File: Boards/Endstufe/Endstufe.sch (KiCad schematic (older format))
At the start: 54 parts, among them J1 HV In, J2 Relais, J3 NF_In, J4 Trafo, K1 G6E, P4 6V3_AC, P6 6V3_DC, P8 Bias, T1 KT88, T2 KT88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

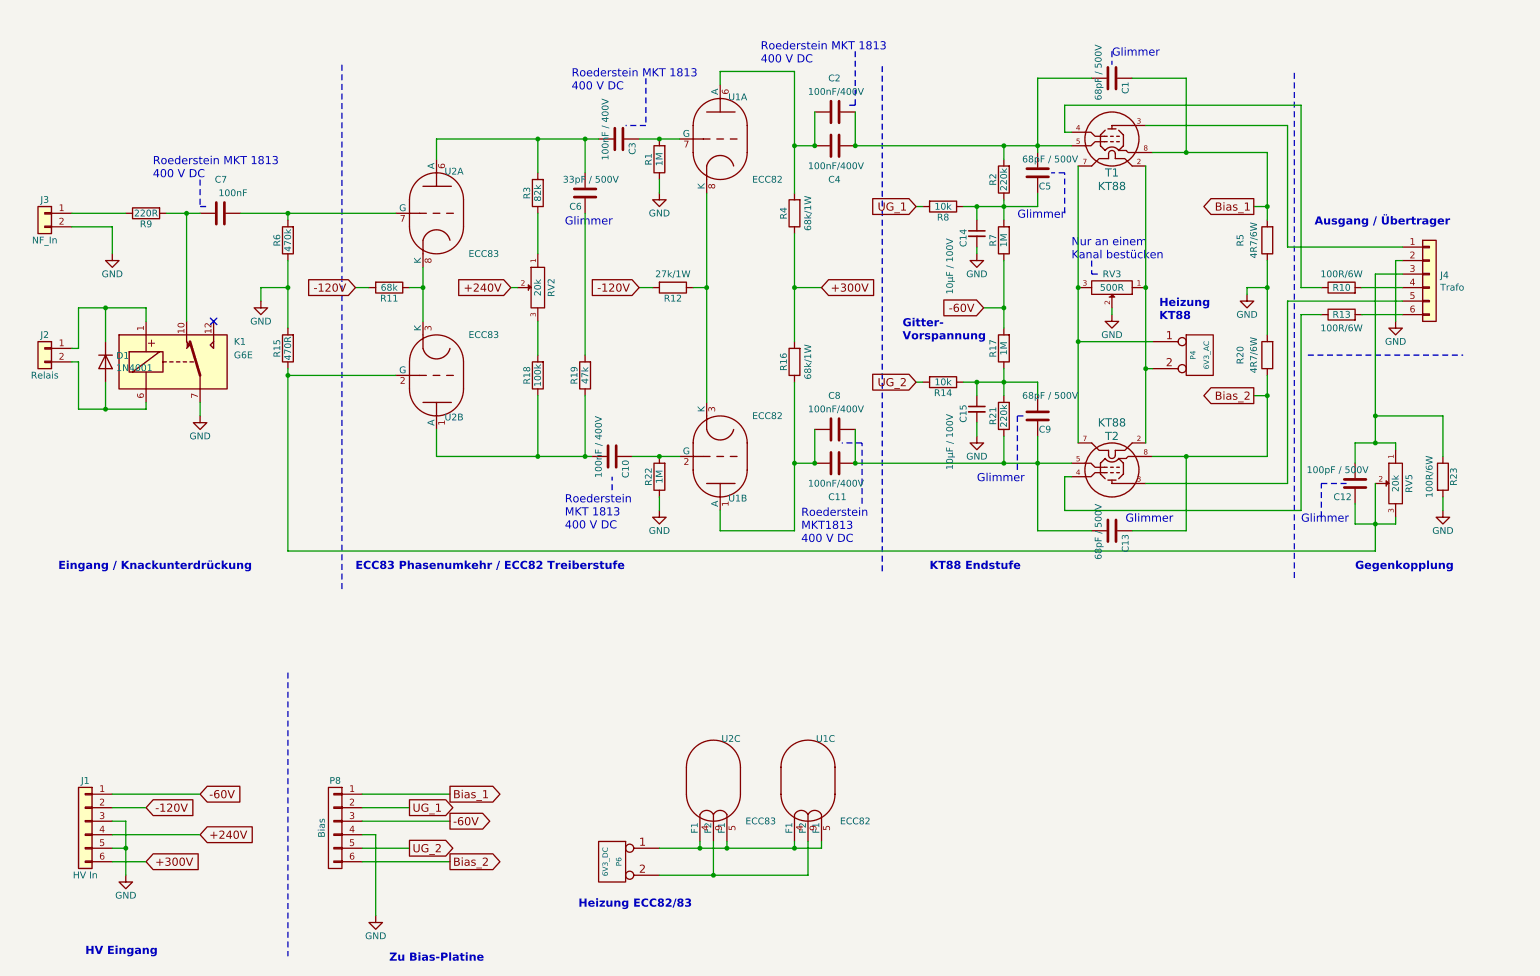
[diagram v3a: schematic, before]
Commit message: Reworked Delay + Layout changed
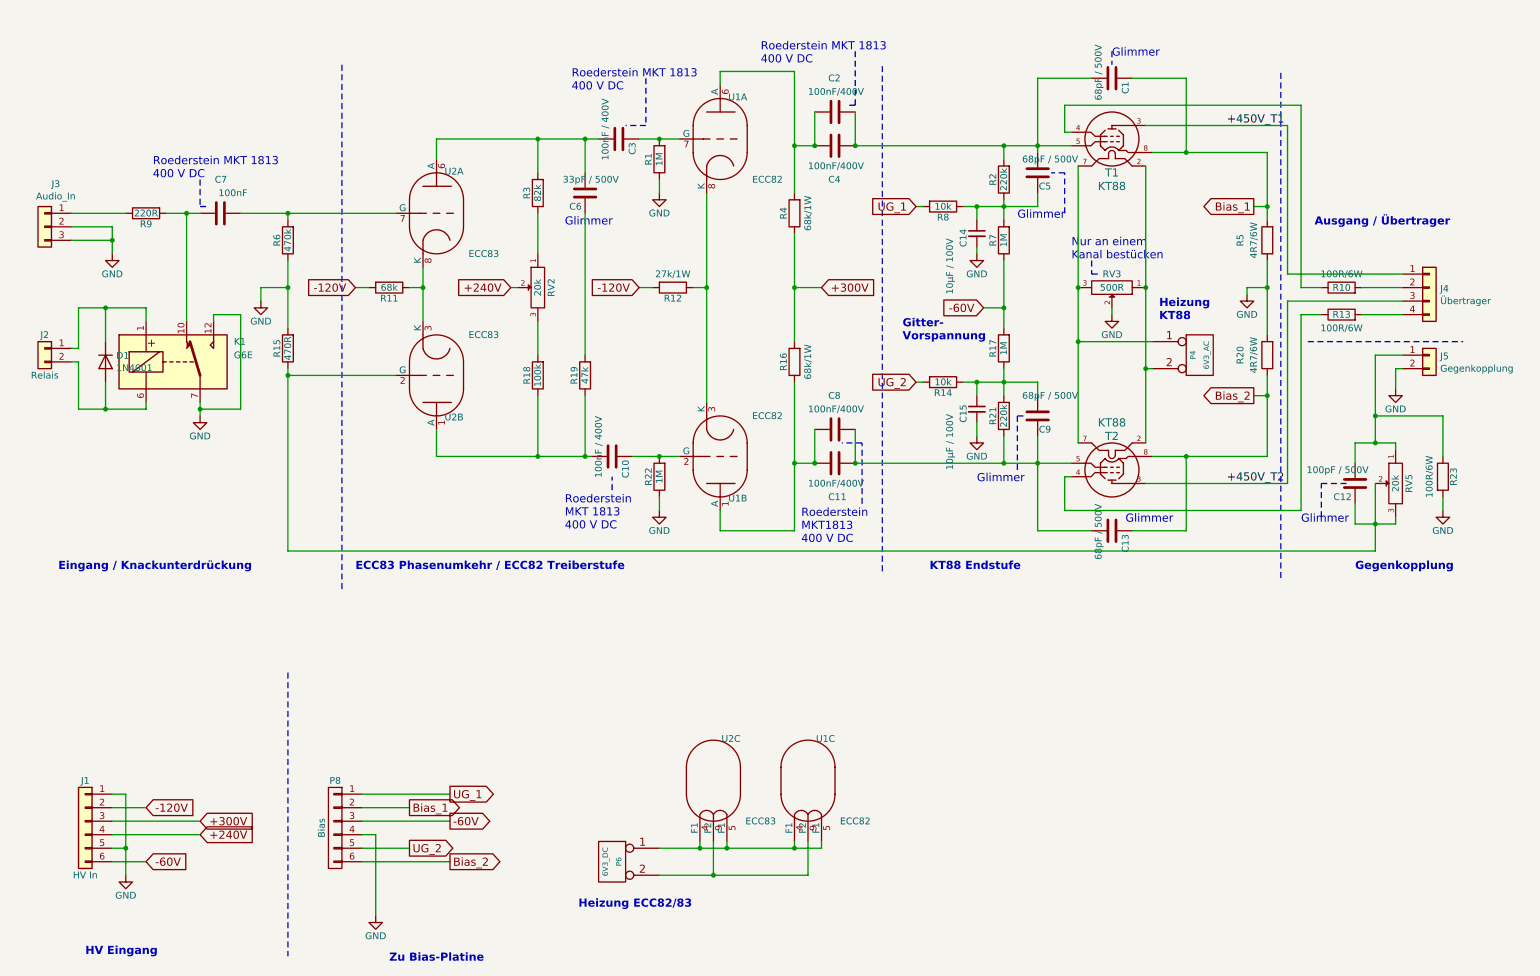
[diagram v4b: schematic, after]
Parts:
- removed J3: NF_In, Connector_JST:JST_EH_B2B-EH-A_1x02_P2.50mm_Vertical, symbol Endstufe-rescue:Conn_01x02
- removed J4: Trafo, Connector_TE-Connectivity:TE_MATE-N-LOK_1-770875-x_2x03_P4.14mm_Vertical, symbol Connector_Generic:Conn_01x06
- added J3: Audio_In, Connector_JST:JST_EH_B3B-EH-A_1x03_P2.50mm_Vertical, symbol Connector_Generic:Conn_01x03
- added J4: Übertrager, Connector_TE-Connectivity:TE_MATE-N-LOK_350211-1_1x04_P5.08mm_Vertical, symbol Connector_Generic:Conn_01x04
- added J5: Gegenkopplung, Connector_TE-Connectivity:TE_MATE-N-LOK_1-770866-x_1x02_P4.14mm_Vertical, symbol Connector_Generic:Conn_01x02
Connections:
- net +300V: now also J1.3 (Pin_3); no longer J1.6 (Pin_6)
- net -60V: now also J1.6 (Pin_6); no longer J1.1 (Pin_1)
- net Bias_1: now also P8.2 (P2); no longer P8.1 (P1)
- net GND: now also J1.1 (Pin_1), K1.12, J3.2 (Pin_2), J3.3 (Pin_3), J5.2 (Pin_2); no longer J1.3 (Pin_3)
- net UG_1: now also P8.1 (P1); no longer P8.2 (P2)
- net +450V_T1: now reaches T1.3 (a)
- net +450V_T1: now also J4.1 (Pin_1)
- net +450V_T2: now reaches T2.3 (a)
- net +450V_T2: now also J4.3 (Pin_3)
- net at C12.2, R23.1, RV5.1: now also J5.1 (Pin_1)
- net at R10.2: now also J4.2 (Pin_2)
- net at R13.2: now also J4.4 (Pin_4)
- net at R9.1: now also J3.1 (Pin_1)
- no-connect marks 1 -> 0
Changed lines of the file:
@@
 Wire Wire Line
 	11050 3600 10550 3600
-Connection ~ 10550 3600
 Wire Wire Line
 	11050 4300 11050 4200
@@
 Connection ~ 5650 7000
 Wire Wire Line
-	1200 2200 1200 2400
-Wire Wire Line
-	900  2200 1200 2200
+	1200 2200 1200 2300
 Wire Notes Line
 	6900 4750 6900 1000
@@
 	1    0    0    -1
 $EndComp
-Text GLabel 1450 6900 2    60   Input ~ 0
+Text GLabel 1850 6600 2    60   Input ~ 0
 +300V
 Text GLabel 1850 6700 2    60   Input ~ 0
@@
 	1    0    0    -1
 $EndComp
-Text GLabel 3400 6500 2    60   Output ~ 0
+Text GLabel 3700 6400 2    60   Output ~ 0
 UG_1
 Text GLabel 3400 6800 2    60   Output ~ 0
 UG_2
-Text GLabel 3700 6400 2    60   Output ~ 0
+Text GLabel 3400 6500 2    60   Output ~ 0
 Bias_1
 Text GLabel 3700 6900 2    60   Output ~ 0
@@
 	2150 2100 2500 2100
 Wire Wire Line
-	3700 6400 3050 6400
-Wire Wire Line
 	3050 6700 3150 6700
 Wire Wire Line
@@
 	1450 3550 1450 3500
 Wire Wire Line
-	1850 3600 1850 3500
+	1850 3600 1850 3550
 $Comp
 L Endstufe-rescue:Conn_01x06 J1
@@
 $EndComp
 $Comp
-L Endstufe-rescue:Conn_01x02 J3
-U 1 1 5A92D98F
-P 700 2100
-F 0 "J3" H 700 2200 50  0000 C CNN
-F 1 "NF_In" H 700 1900 50  0000 C CNN
-F 2 "Connector_JST:JST_EH_B2B-EH-A_1x02_P2.50mm_Vertical" H 700 2100 50  0001 C CNN
-F 3 "" H 700 2100 50  0001 C CNN
-	1    700  2100
-	-1   0    0    -1
-$EndComp
-$Comp
 L Endstufe-rescue:Conn_01x02 J2
 U 1 1 5A92DE06
@@
 Wire Wire Line
 	9750 3450 9750 3900
-NoConn ~ 1950 2900
 Wire Wire Line
 	1750 2100 1850 2100
@@
 Connection ~ 6700 1600
 Connection ~ 6700 3950
-$Comp
-L Connector_Generic:Conn_01x06 J4
-U 1 1 5CC18566
-P 10950 2550
-F 0 "J4" H 11030 2542 50  0000 L CNN
-F 1 "Trafo" H 11030 2451 50  0000 L CNN
-F 2 "Connector_TE-Connectivity:TE_MATE-N-LOK_1-770875-x_2x03_P4.14mm_Vertical" H 10950 2550 50  0001 C CNN
-F 3 "~" H 10950 2550 50  0001 C CNN
-	1    10950 2550
-	1    0    0    -1
-$EndComp
-Wire Wire Line
-	9900 1450 9900 2350
-Wire Wire Line
-	10750 2350 9900 2350
+Wire Wire Line
+	9900 1450 9900 2550
+Wire Wire Line
+	10750 2550 9900 2550
 Wire Wire Line
 	10450 2650 10750 2650
-$Comp
-L Endstufe-rescue:GND #PWR0101
-U 1 1 5CCAF2A5
-P 10700 2900
-F 0 "#PWR0101" H 10700 2650 50  0001 C CNN
-F 1 "GND" H 10700 2750 50  0000 C CNN
-F 2 "" H 10700 2900 60  0000 C CNN
-F 3 "" H 10700 2900 60  0000 C CNN
-	1    10700 2900
-	1    0    0    -1
-$EndComp
-Wire Wire Line
-	10700 2450 10750 2450
-Wire Wire Line
-	10700 2450 10700 2900
 Wire Wire Line
 	10750 2850 10450 2850
@@
 Heizung\nKT88
 Wire Notes Line
-	9950 4800 9950 1050
-Wire Notes Line
-	10050 3150 11200 3150
+	9850 4800 9850 1050
+Wire Notes Line
+	10050 3050 11200 3050
 Wire Notes Line
 	2500 5500 2500 7600
@@
 Wire Wire Line
 	3050 6800 3400 6800
-Wire Wire Line
-	3050 6500 3400 6500
 Wire Wire Line
 	7600 2400 7600 2350
@@
 	1450 6500 1200 6500
 Wire Wire Line
-	1200 6600 1300 6600
-Wire Wire Line
-	1300 6600 1300 6800
-Wire Wire Line
 	1200 6800 1300 6800
-Connection ~ 1300 6800
 Wire Wire Line
 	1300 6800 1300 7000
-Text GLabel 1850 6400 2    60   Input ~ 0
+Text GLabel 1450 6900 2    60   Input ~ 0
 -60V
-Wire Wire Line
-	1850 6400 1200 6400
 Wire Wire Line
 	7800 2450 7800 2800
@@
 Wire Notes Line
 	8450 2550 8500 2550
-Wire Wire Line
-	10550 2550 10750 2550
-Wire Wire Line
-	10550 2550 10550 3600
+$Comp
+L Connector_Generic:Conn_01x04 J4
+U 1 1 60906A39
+P 10950 2650
+F 0 "J4" H 11030 2642 50  0000 L CNN
+F 1 "Übertrager" H 11030 2551 50  0000 L CNN
+F 2 "Connector_TE-Connectivity:TE_MATE-N-LOK_350211-1_1x04_P5.08mm_Vertical" H 10950 2650 50  0001 C CNN
+F 3 "~" H 10950 2650 50  0001 C CNN
+	1    10950 2650
+	1    0    0    -1
+$EndComp
+$Comp
+L Connector_Generic:Conn_01x02 J5
+U 1 1 60914273
+P 10950 3150
+F 0 "J5" H 11030 3142 50  0000 L CNN
+F 1 "Gegenkopplung" H 11030 3051 50  0000 L CNN
+F 2 "Connector_TE-Connectivity:TE_MATE-N-LOK_1-770866-x_1x02_P4.14mm_Vertical" H 10950 3150 50  0001 C CNN
+F 3 "~" H 10950 3150 50  0001 C CNN
+	1    10950 3150
+	1    0    0    -1
+$EndComp
+Connection ~ 10550 3600
+$Comp
+L Endstufe-rescue:GND #PWR0101
+U 1 1 60920978
+P 10700 3400
+F 0 "#PWR0101" H 10700 3150 50  0001 C CNN
+F 1 "GND" H 10700 3250 50  0000 C CNN
+F 2 "" H 10700 3400 60  0000 C CNN
+F 3 "" H 10700 3400 60  0000 C CNN
+	1    10700 3400
+	1    0    0    -1
+$EndComp
+Wire Wire Line
+	10750 3150 10550 3150
+Wire Wire Line
+	10550 3150 10550 3600
+Wire Wire Line
+	10750 3250 10700 3250
+Wire Wire Line
+	10700 3250 10700 3400
+Wire Wire Line
+	1850 6600 1200 6600
+Wire Wire Line
+	1300 6800 1300 6400
+Wire Wire Line
+	1300 6400 1200 6400
+Connection ~ 1300 6800
+Wire Wire Line
+	3400 6500 3050 6500
+Wire Wire Line
+	3050 6400 3700 6400
+Wire Wire Line
+	1850 3550 2150 3550
+Wire Wire Line
+	2150 3550 2150 2850
+Wire Wire Line
+	2150 2850 1950 2850
+Wire Wire Line
+	1950 2850 1950 2900
+Connection ~ 1850 3550
+Wire Wire Line
+	1850 3550 1850 3500
+$Comp
+L Connector_Generic:Conn_01x03 J3
+U 1 1 6099AC4C
+P 700 2200
+F 0 "J3" H 618 2517 50  0000 C CNN
+F 1 "Audio_In" H 618 2426 50  0000 C CNN
+F 2 "Connector_JST:JST_EH_B3B-EH-A_1x03_P2.50mm_Vertical" H 700 2200 50  0001 C CNN
+F 3 "~" H 700 2200 50  0001 C CNN
+	1    700  2200
+	-1   0    0    -1
+$EndComp
+Wire Wire Line
+	900  2300 1200 2300
+Connection ~ 1200 2300
+Wire Wire Line
+	1200 2300 1200 2400
+Wire Wire Line
+	1200 2200 900  2200
+Text Label 9450 1450 0    60   ~ 0
++450V_T1
+Text Label 9450 4100 0    60   ~ 0
++450V_T2
 $EndSCHEMATC

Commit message: Work in progess - many LAyour changes
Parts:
- removed C14, C15: 10µF / 100V, Capacitor_THT:C_Radial_D6.3mm_H5.0mm_P2.50mm, symbol Endstufe-rescue:C_Small
- removed P4: 6V3_AC, Connector_TE-Connectivity:TE_MATE-N-LOK_1-770866-x_1x02_P4.14mm_Vertical, symbol Endstufe-rescue:CONN_2
- removed P8: Bias, Connector_PinHeader_2.54mm:PinHeader_2x03_P2.54mm_Vertical, symbol Endstufe-rescue:CONN_01X06
- removed RV3: 500R, Potentiometer_THT:Potentiometer_Piher_PT-10-V10_Vertical, symbol Endstufe-rescue:POT-RESCUE-Endstufe
- added C14, C15: 10µF/100V, Capacitor_THT:CP_Radial_D6.3mm_P2.50mm, symbol Device:CP_Small
- added J10: 240V VU, Connector_TE-Connectivity:TE_MATE-N-LOK_1-770866-x_1x02_P4.14mm_Vertical, symbol Connector_Generic:Conn_01x02
- added J6: 12V out, Connector_Molex:Molex_KK-254_AE-6410-02A_1x02_P2.54mm_Vertical, symbol Connector_Generic:Conn_01x02
- added J7: Conn_01x08, Connector_PinHeader_2.54mm:PinHeader_2x04_P2.54mm_Vertical, symbol Connector_Generic:Conn_01x08
- added J8: 12V In, Connector_Molex:Molex_KK-254_AE-6410-02A_1x02_P2.54mm_Vertical, symbol Connector_Generic:Conn_01x02
- added J9: VU-Meter, Connector_TE-Connectivity:TE_MATE-N-LOK_1-770866-x_1x02_P4.14mm_Vertical, symbol Connector_Generic:Conn_01x02
- added P1, P2: 6V3_AC, Connector_TE-Connectivity:TE_MATE-N-LOK_1-770866-x_1x02_P4.14mm_Vertical, symbol Endstufe-rescue:CONN_2
- C6: footprint Capacitor_THT:C_Disc_D6.0mm_W2.5mm_P5.00mm -> Capacitor_THT:C_Disc_D6.0mm_W4.4mm_P5.00mm
- C7: footprint Capacitor_THT:C_Disc_D3.0mm_W2.0mm_P2.50mm -> Capacitor_THT:C_Axial_L22.0mm_D9.5mm_P27.50mm_Horizontal
- C9: footprint Capacitor_THT:C_Disc_D7.5mm_W2.5mm_P5.00mm -> Capacitor_THT:C_Disc_D7.5mm_W4.4mm_P5.00mm
- R10, R13, R20, R23, R5: footprint Resistor_THT:R_Axial_Power_L25.0mm_W9.0mm_P30.48mm -> Resistor_THT:R_Axial_DIN0922_L20.0mm_D9.0mm_P25.40mm_Horizontal
- R11: value 68k -> 68k/1W; footprint Resistor_THT:R_Axial_DIN0207_L6.3mm_D2.5mm_P10.16mm_Horizontal -> Resistor_THT:R_Axial_DIN0207_L6.3mm_D2.5mm_P15.24mm_Horizontal
- R12: footprint Resistor_THT:R_Axial_DIN0414_L11.9mm_D4.5mm_P20.32mm_Horizontal -> Resistor_THT:R_Axial_DIN0207_L6.3mm_D2.5mm_P15.24mm_Horizontal
- R16, R4: footprint Resistor_THT:R_Axial_DIN0414_L11.9mm_D4.5mm_P15.24mm_Horizontal -> Resistor_THT:R_Axial_DIN0207_L6.3mm_D2.5mm_P10.16mm_Horizontal
- RV2, RV5: footprint Potentiometer_THT:Potentiometer_Piher_PT-10-V10_Vertical -> Potentiometer_THT:Potentiometer_Piher_PT-10-V10_Vertical_Hole
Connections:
- net +240V: now also J10.1 (Pin_1)
- net +450V_T1: now also J9.1 (Pin_1)
- net -60V: now also J7.3 (Pin_3)
- net Bias_1: now also J7.2 (Pin_2)
- net Bias_2: now also J7.6 (Pin_6)
- net GND: now also C14.2, C15.2, J10.2 (Pin_2), J6.2 (Pin_2), J7.4 (Pin_4), J7.7 (Pin_7), J8.2 (Pin_2), J9.2 (Pin_2)
- net UG_1: now also J7.1 (Pin_1)
- net UG_2: now also J7.5 (Pin_5)
- net at T1.2 (f): now also P1.1 (P1); no longer T2.2 (f)
- net at T1.7 (f): now also P1.2 (P2); no longer T2.7 (f)
- net at C12.1, R15.1, RV5.3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: no longer RV5.2
- net at P6.1 (P1), U2.4 (F1), U2.5 (F1): now also U1.9 (F2); no longer U1.4 (F1), U1.5 (F1)
- net at P6.2 (P2), U2.9 (F2): now also U1.4 (F1), U1.5 (F1); no longer U1.9 (F2)
- net at RV2.1: now also R18.2; no longer R3.1
- net at RV2.3: now also R3.1; no longer R18.2
- net at C5.1, R2.1, R7.2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: now also C14.1
- net at C9.2, R14.1, R17.1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: now also C15.1
- net at C12.2, J5.1 (Pin_1), R23.1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: now also RV5.2
- new net: P2.1 (P1), T2.2 (f)
- new net: P2.2 (P2), T2.7 (f)
- new net +12V: J6.1 (Pin_1), J7.8 (Pin_8), J8.1 (Pin_1)
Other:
- note added: "12V Ein-/Ausgang"
- note added: "Abgleich von RV2\nStecker für Ausgangsübertrager ziehen. Verstärker\nmit 1kHz Sinus ansteuern\nAuf einheitliche Sinuskurve mit minimaler Amplitude an\nKathode von U1A/B einstellen"
- note added: "Ausgang / \nÜbertrager"
- note added: "ECC83 Phasensplitter / ECC82 Treiberstufe"
- note added: "Gegenkopplung:\nAn 4 Ohm Ausgang des Übertragers\nVerhältnis U an 8 Ohm-Ausgang zu U an Steuergitter U2B auf 19,5 dB"
- note added: "Roederstein\nMKT 1813\n400 V DC"
- note removed: "Ausgang / Übertrager"
- note removed: "ECC83 Phasenumkehr / ECC82 Treiberstufe"
- note removed: "Nur an einem \nKanal bestücken"
- note removed: "Roederstein MKT 1813\n400 V DC"
- moved on the sheet: C1, C10, C11, C12, C13, C2, C3, C4, C5, C6, C7, C8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
